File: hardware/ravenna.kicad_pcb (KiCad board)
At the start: 4 copper layers, 22.9 x 71.9 mm, 68 parts, among them IC2 FT232H, IC3 MCP1755, IC4 93C56, IC5 RAVENAQFN56, J7 47491-0001, J9 2X6 FEMALE, U2 W25Q32FV, X1 12MHZ, X2 8MHZ

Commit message: parts libraries
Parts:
- removed C1, C14, C2, C3: 27pf, C0201
- removed C23: 2.2uf, C0201
- removed C7: 1uf, C0201
- removed G***: LOGO, raptor-KiCadVersion:logo
- removed IC5: RAVENAQFN56, QFN56
- removed J10, J6: , 1X02
- removed J11, J12: , 1X20
- removed J7: 47491-0001, 47491-0001
- removed J9: 2X6 FEMALE, 2X6
- removed RESET: SPST-SMD-4.6X2.8mm, TACTILE_SWITCH_SMD_4.6X2.8MM
- removed U$4: MCP1811, SOT23
- added IC1: RAVENAQFN56, parts and footprints:QFN56, F.Cu at (148.3, 115.2)
- added J1: 629105150521, parts and footprints:629105150521, F.Cu at (148.5, 88.8)
- added R10: 10K, parts and footprints:R_0603_1608Metric, B.Cu at (142.8, 127.4)
- added R11: 10K, parts and footprints:R_0603_1608Metric, B.Cu at (145.8, 128.9)
- added R15: 10K, parts and footprints:R_0603_1608Metric, B.Cu at (142.8, 125.9)
- added R16: 10K, parts and footprints:R_0603_1608Metric, B.Cu at (145.8, 127.4)
- added R22: 0, Resistor_SMD:R_0603_1608Metric, F.Cu at (151.0, 79.9)
- added R23: 10K, Resistor_SMD:R_0603_1608Metric, F.Cu at (155.3, 79.9)
- added R3: 10K, parts and footprints:R_0603_1608Metric, B.Cu at (142.8, 128.9)
- added REF**: CSTNE12M0GH5L000R0, parts and footprints:CSTNE12M0GH5L000R0, B.Cu at (142.6, 100.5)
- added RESET1: SPST-SMD-4.6X2.8mm, parts and footprints:TACTILE_SWITCH_SMD_4.6X2.8MM, F.Cu at (143.6, 94.1)
- added U1: SN74LVC1G125DCKR, parts and footprints:SC-70-5, B.Cu at (149.6, 126.7)
- C15, C16, C17, C18, C19, C20, C21, C22, C27, C28, C29, C30, C4, C5, C8, C9: footprint C0201 -> Capacitor_SMD:C_0603_1608Metric
- J2: value (none) -> Conn_01x02_Male; footprint 1X03 -> Connector_PinHeader_2.54mm:PinHeader_1x02_P2.54mm_Vertical
- J3: value (none) -> 2X6 FEMALE; footprint 1X03 -> Connector_PinHeader_2.54mm:PinHeader_2x06_P2.54mm_Vertical
- J4, J5: value (none) -> CONN_20; footprint 1X03 -> Connector_PinHeader_2.54mm:PinHeader_1x20_P2.54mm_Vertical
- LED10, LED11, LED12, LED13, LED14, LED8, LED9: value (none) -> LEDCHIPLED_0603
- R1, R12, R13, R17, R18, R19, R20, R21, R4, R5, R6, R7, R8: footprint R0201 -> Resistor_SMD:R_0603_1608Metric
- R14, R2: value 4.7K -> 10K; footprint R0201 -> Resistor_SMD:R_0603_1608Metric
- R9: value 2K 1% -> 12K 1%; footprint R0201 -> Resistor_SMD:R_0603_1608Metric
- U2: moved to F.Cu
- X1: value 12MHZ -> 12MHz; footprint 445I23D24M00000 -> parts and footprints:CSTNE12M0GH5L000R0
- X2: value 8MHZ -> 6 MHz; footprint CX8045GA04000H0PST03 -> CSTNE12M0GH5L000R0
- moved J3 56.0 mm to (154.8, 131.4), turned to 270 degrees
- moved J2 42.5 mm to (154.8, 125.5), turned to 0 degrees
- moved J5 20.0 mm to (158.4, 85.7), turned to 0 degrees
- moved U2 19.8 mm to (145.5, 102.0), turned to 270 degrees
- moved R12 18.5 mm to (156.1, 96.6), turned to 90 degrees
- moved C27 17.3 mm to (142.5, 107.0), turned to 90 degrees
- moved C19 16.8 mm to (144.2, 107.0), turned to 90 degrees
- moved C5 15.8 mm to (156.1, 94.1)
- moved C9 13.6 mm to (153.8, 98.2), turned to 180 degrees
- moved U$1 13.1 mm to (153.6, 95.2)
- moved C4 12.9 mm to (152.5, 92.6), turned to 180 degrees
- moved IC3 12.7 mm to (148.5, 95.1)
- moved X2 12.3 mm to (155.6, 109.4)
- moved FUSE_0 12.0 mm to (144.7, 93.5)
- moved R4 12.0 mm to (155.6, 91.8), turned to 270 degrees
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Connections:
- C15 pad 2: +3V3 -> +5V
- C16 pad 1: +3V3 -> +5V
- C17 pad 1: +3V3 -> +5V
- C19 pad 1: VDD(3.3) -> +5V
- C20 pad 1: +3V3 -> +5V
- C21 pad 1: +3V3 -> +5V
- C29 pad 2: VDD(3.3) -> +5V
- C5 pad 2: +3V3 -> +5V
- C9 pad 1: VDD(3.3) -> +5V
- IC2 pad 12: +3V3 -> +5V
- IC2 pad 13: USB_SCK_TXD -> /TXD_HK_SCK
- IC2 pad 14: USB_SO_RXD -> /RXD_HK_SDI
- IC2 pad 15: USB_SI -> /HK_SDO
- IC2 pad 16: USB_CS -> /HK_CSB
- IC2 pad 17: (no net) -> Net-(IC2-Pad17)
- IC2 pad 18: (no net) -> Net-(IC2-Pad18)
- IC2 pad 19: (no net) -> Net-(IC2-Pad19)
- IC2 pad 2: N$11 -> Net-(IC2-Pad2)
- IC2 pad 20: (no net) -> Net-(IC2-Pad20)
- IC2 pad 21: (no net) -> /TMUX_SEL
- IC2 pad 24: +3V3 -> +5V
- IC2 pad 25: (no net) -> /TXD_EN
- IC2 pad 26: (no net) -> Net-(IC2-Pad26)
- IC2 pad 27: (no net) -> Net-(IC2-Pad27)
- IC2 pad 28: (no net) -> Net-(IC2-Pad28)
- IC2 pad 29: (no net) -> Net-(IC2-Pad29)
- IC2 pad 3: +3V3 -> +5V
- IC2 pad 30: (no net) -> Net-(IC2-Pad30)
- IC2 pad 31: N$27 -> Net-(IC2-Pad31)
- IC2 pad 39: +3V3 -> +5V
- IC2 pad 44: N$8 -> Net-(IC2-Pad44)
- IC2 pad 46: +3V3 -> +5V
- IC2 pad 8: +3V3 -> +5V
- IC3 pad 4: (no net) -> Net-(IC3-Pad4)
- IC3 pad 5: VDD(3.3) -> +5V
- IC4 pad 4: N$8 -> Net-(IC2-Pad44)
- IC4 pad 6: +3V3 -> +5V
- J2 pad 1: RAPTOR_CS -> GND
- J2 pad 2: N$14 -> /TXD_EN
- J3 pad 1: RAPTOR_D1 -> /SPI_CSB
- J3 pad 2: N$15 -> /P0
- J3 pad 3: USB_SI -> /SPI_SDO
- J4 pad 1: RAPTOR_SCK -> +5V
- J4 pad 2: N$17 -> /P8
- J4 pad 3: USB_SCK_TXD -> /P9
- J5 pad 1: RAPTOR_D0 -> /XCLK
- J5 pad 2: N$16 -> /P0
- J5 pad 3: USB_SO_RXD -> /P1
- R1 pad 1: RAPTOR_D2 -> +5V
- R1 pad 2: +3V3 -> /RAPTOR_D2
- R12 pad 1: RAPTOR_D3 -> +5V
- R12 pad 2: +3V3 -> /RAPTOR_D3
- R13 pad 1: GND -> +5V
- R14 pad 1: N$27 -> +5V
- R14 pad 2: +5V -> Net-(IC2-Pad44)
- R17 pad 2: VDD(3.3) -> +5V
- R18 pad 2: P0 -> /P0
- R19 pad 2: P1 -> /P1
- R2 pad 1: GND -> +5V
- R2 pad 2: N$27 -> /RAPTOR_CS
- R20 pad 2: P2 -> /P2
- R21 pad 2: P3 -> /P3
- R5 pad 2: +3V3 -> +5V
- R6 pad 1: GND -> +5V
- R8 pad 1: IRQ -> /IRQ
- U$1 pad 5: (no net) -> Net-(U$1-Pad5)
- U2 pad 1: N$14 -> /RAPTOR_CS
- U2 pad 2: N$15 -> /RAPTOR_D1
- U2 pad 3: RAPTOR_D2 -> /RAPTOR_D2
- U2 pad 5: N$16 -> /RAPTOR_D0
- U2 pad 6: N$17 -> /RAPTOR_SCK
- U2 pad 7: RAPTOR_D3 -> /RAPTOR_D3
- U2 pad 8: +3V3 -> +5V
- X1 pad 2: N$11 -> GND
- X2 pad 2: N$10 -> GND
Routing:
- net GND: track 226.6 -> 116.2 mm, vias 12 -> 3
- net VDD(3.3): track 109.2 -> 0.00 mm, vias 3 -> 0
- net /P2: track 0.00 -> 99.8 mm, vias 0 -> 1
- net +3V3: track 77.3 -> 0.00 mm, vias 5 -> 0
- net RX0: track 75.1 -> 0.00 mm, vias 3 -> 0
- net RAPTOR_D1: track 73.9 -> 0.00 mm, vias 1 -> 0
- net TX0: track 68.2 -> 0.00 mm, vias 3 -> 0
- net /XCLK: track 0.00 -> 64.0 mm, vias 0 -> 1
- net RAPTOR_SCK: track 62.8 -> 0.00 mm, vias 1 -> 0
- net P1: track 61.9 -> 0.00 mm, vias 3 -> 0
- net RAPTOR_CS: track 61.8 -> 0.00 mm, vias 2 -> 0
- net P0: track 61.7 -> 0.00 mm, vias 3 -> 0
- net (no net): track 0.00 -> 61.0 mm, vias 0 -> 3
- net /SPI_CSB: track 0.00 -> 60.5 mm, vias 0 -> 2
- net RAPTOR_D3: track 55.7 -> 0.00 mm, vias 2 -> 0
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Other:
- board size 22.9 x 71.9 mm -> 22.9 x 51.4 mm
- board text added: "A00"
- board text added: "A01"
- board text added: "CIN_N"
- board text added: "CIN_P"
- board text removed: "ANA_0"
- board text removed: "ANA_1"
- board text removed: "COMP_INN"
- board text removed: "COMP_INP"
- board text removed: "RCS"
- board text removed: "RD0"
- board text removed: "RD1"
- board text removed: "RSck"
- board text removed: "RX0>"
- board text removed: "SPI_SDI"
- board text removed: "SPI_SDO"
- board text removed: "TX0>"
- board text removed: "USB_CS"
- board text removed: "USB_SCK_TXD<>"
- board text removed: "USB_SI"
- board text removed: "USB_SO_RXD<>"

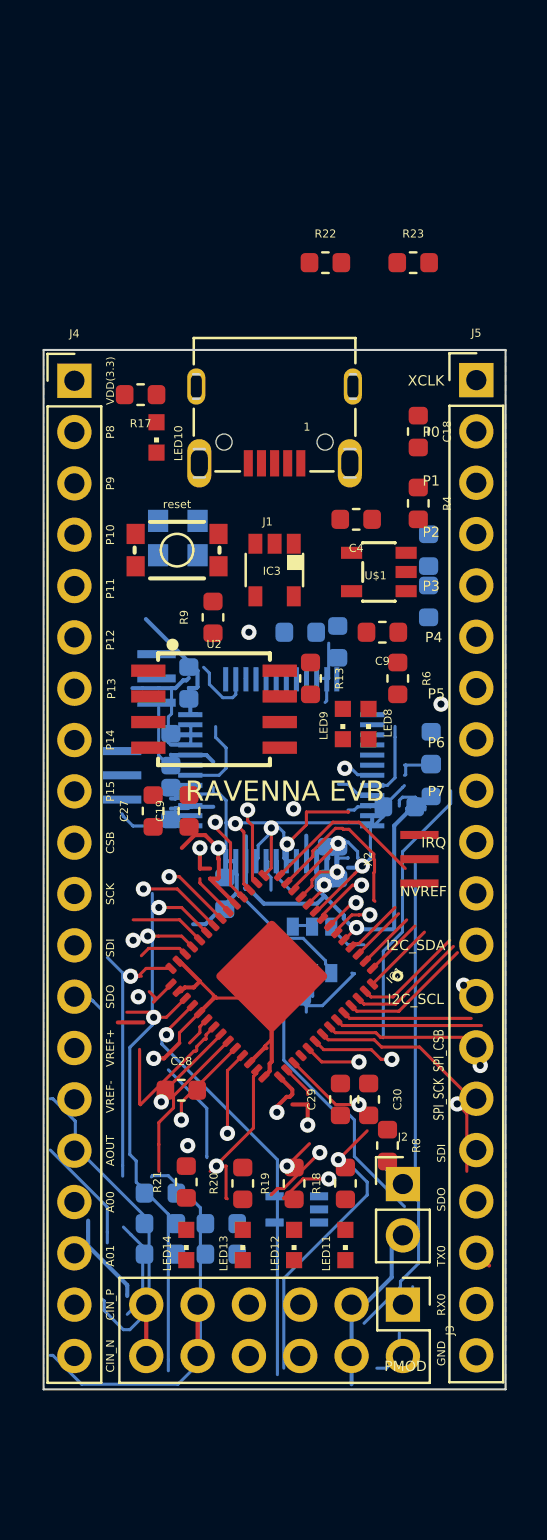
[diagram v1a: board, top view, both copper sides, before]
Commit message: completed revised layout
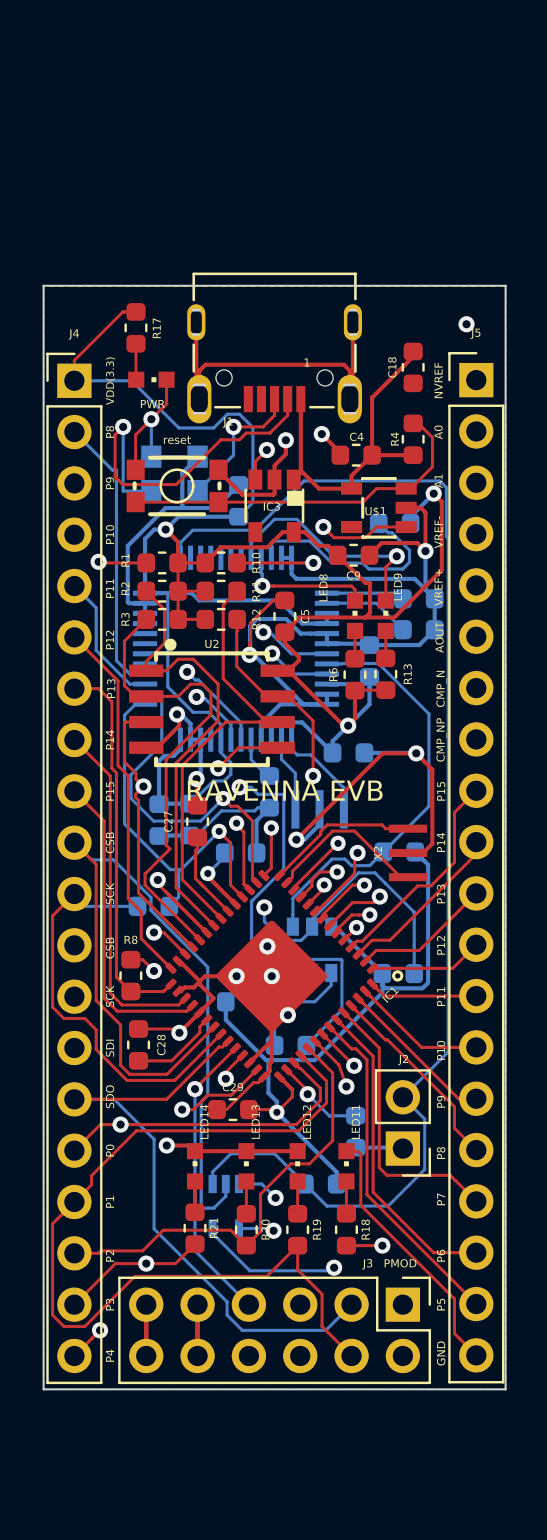
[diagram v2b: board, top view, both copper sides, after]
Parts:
- removed REF**: CSTNE12M0GH5L000R0, parts and footprints:CSTNE12M0GH5L000R0
- C19, C30, R22, R23, R9: moved to B.Cu
- C5, R1, R10, R11, R12, R2, R3: moved to F.Cu
- moved R23 45.8 mm to (150.7, 125.5)
- moved R22 33.0 mm to (142.5, 111.7), turned to 180 degrees
- moved R10 32.8 mm to (145.8, 94.7)
- moved R11 32.8 mm to (145.8, 96.1)
- moved R3 31.4 mm to (142.9, 97.5), turned to 180 degrees
- moved R2 16.3 mm to (142.9, 96.1), turned to 180 degrees
- moved R15 16.0 mm to (154.6, 115.1)
- moved R8 15.2 mm to (141.4, 115.2), turned to 90 degrees
- moved R5 14.0 mm to (154.4, 92.8)
- moved C8 13.8 mm to (155.6, 96.5), turned to 180 degrees
- moved C17 13.5 mm to (153.2, 99.6), turned to 90 degrees
- moved C22 12.2 mm to (155.6, 98.0), turned to 180 degrees
- moved R16 11.0 mm to (146.8, 116.5)
- moved R12 10.3 mm to (145.8, 97.5), turned to 0 degrees
- moved X1 9.92 mm to (150.7, 106.9), turned to 0 degrees
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- renumbered FUSE_0 to FUSE0
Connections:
- C15 pad 2: +5V -> VDD
- C16 pad 1: +5V -> VDD
- C17 pad 1: +5V -> VDD
- C19 pad 1: +5V -> VDD
- C20 pad 1: +5V -> VDD
- C21 pad 1: +5V -> VDD
- C29 pad 2: +5V -> VDD
- C5 pad 2: +5V -> VDD
- C9 pad 1: +5V -> VDD
- IC1 pad 19: +5V -> VDD
- IC1 pad 43: +5V -> VDD
- IC2 pad 12: +5V -> VDD
- IC2 pad 24: +5V -> VDD
- IC2 pad 3: +5V -> VDD
- IC2 pad 39: +5V -> VDD
- IC2 pad 40: +5V -> VDD
- IC2 pad 46: +5V -> VDD
- IC2 pad 8: +5V -> VDD
- IC3 pad 5: +5V -> VDD
- IC4 pad 6: +5V -> VDD
- J3 pad 11: +5V -> VDD
- J3 pad 12: +5V -> VDD
- J4 pad 1: +5V -> VDD
- J4 pad 10: /HK_CSB -> /TX0
- J4 pad 11: /TXD_HK_SCK -> /RX0
- J4 pad 12: /RXD_HK_SDI -> /SPI_CSB
- J4 pad 13: /HK_SDO -> /SPI_SCK
- J4 pad 14: /VREF+ -> /SPI_SDI
- J4 pad 15: /VREF- -> /SPI_SDO
- J4 pad 16: /AOUT -> /P0
- J4 pad 17: /ANA_0 -> /P1
- J4 pad 18: /ANA_1 -> /P2
- J4 pad 19: /COMP_INP -> /P3
- J4 pad 2: /P8 -> /HK_CSB
- J4 pad 20: /COMP_INN -> /P4
- J4 pad 3: /P9 -> /TXD_HK_SCK
- J4 pad 4: /P10 -> /RXD_HK_SDI
- J4 pad 5: /P11 -> /HK_SDO
- J4 pad 6: /P12 -> /XCLK
- J4 pad 7: /P13 -> /IRQ
- J4 pad 8: /P14 -> /I2C_SDA
- J4 pad 9: /P15 -> /I2C_SCL
- J5 pad 1: /XCLK -> /NVREF
- J5 pad 10: /IRQ -> /P14
- J5 pad 11: /NVREF -> /P13
- J5 pad 12: /I2C_SDA -> /P12
- J5 pad 13: /I2C_SCL -> /P11
- J5 pad 14: /SPI_CSB -> /P10
- J5 pad 15: /SPI_SCK -> /P9
- J5 pad 16: /SPI_SDI -> /P8
- J5 pad 17: /SPI_SDO -> /P7
- J5 pad 18: /TX0 -> /P6
- J5 pad 19: /RX0 -> /P5
- J5 pad 2: /P0 -> /ANA_0
- J5 pad 3: /P1 -> /ANA_1
- J5 pad 4: /P2 -> /VREF-
- J5 pad 5: /P3 -> /VREF+
- J5 pad 6: /P4 -> /AOUT
- J5 pad 7: /P5 -> /COMP_INN
- J5 pad 8: /P6 -> /COMP_INP
- J5 pad 9: /P7 -> /P15
- R1 pad 1: +5V -> VDD
- R10 pad 1: +5V -> VDD
- R11 pad 1: +5V -> VDD
- R12 pad 1: +5V -> VDD
- R13 pad 1: +5V -> VDD
- R14 pad 1: +5V -> VDD
- R15 pad 1: +5V -> VDD
- R16 pad 1: +5V -> VDD
- R17 pad 2: +5V -> VDD
- R2 pad 1: +5V -> VDD
- R23 pad 2: +5V -> VDD
- R3 pad 1: +5V -> VDD
- R5 pad 2: +5V -> VDD
- R6 pad 1: +5V -> VDD
- U1 pad 5: +5V -> VDD
- U2 pad 8: +5V -> VDD
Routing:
- net VDD: track 0.00 -> 219.7 mm, vias 0 -> 6
- net GND: track 116.2 -> 241.9 mm, vias 3 -> 18
- net /P2: track 99.8 -> 21.9 mm, vias 1 -> 0
- net +5V: track 85.5 -> 17.4 mm, vias 3 -> 0
- net /RXD_HK_SDI: track 7.14 -> 73.8 mm, vias 1 -> 2
- net /TXD_EN: track 0.00 -> 63.8 mm
- net (no net): track 61.0 -> 0.21 mm, vias 3 -> 0
- net /XCLK: track 64.0 -> 18.4 mm, vias 1 -> 0
- net /P1: track 3.35 -> 44.3 mm, vias 2 -> 0
- net /P10: track 45.5 -> 7.27 mm
- net /SPI_CSB: track 60.5 -> 26.8 mm, vias 2 -> 1
- net Net-(FUSE1-Pad2): track 4.19 -> 36.4 mm, vias 0 -> 2
- net /AOUT: track 47.6 -> 17.9 mm
- net Net-(IC2-Pad45): track 1.49 -> 30.6 mm, vias 0 -> 2
- net /RAPTOR_D2: track 2.44 -> 28.3 mm, vias 1 -> 2
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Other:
- board size 22.9 x 51.4 mm -> 22.9 x 54.6 mm
- board text added: "A0"
- board text added: "A1"
- board text added: "CMP_N"
- board text added: "CMP_NP"
- board text added: "PWR"
- board text removed: "A00"
- board text removed: "A01"
- board text removed: "CIN_N"
- board text removed: "CIN_P"
- board text removed: "I2C_SCL"
- board text removed: "I2C_SDA"
- board text removed: "IRQ"
- board text removed: "RX0"
- board text removed: "SPI_CSB"
- board text removed: "SPI_SCK"
- board text removed: "TX0"
- board text removed: "XCLK"
